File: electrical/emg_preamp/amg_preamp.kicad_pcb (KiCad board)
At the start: 2 copper layers, 29 x 13.5 mm, 26 parts, among them J1 in, J2 T1, J3 T2, J4 Conn_01x05, U1 TSZ124IPT

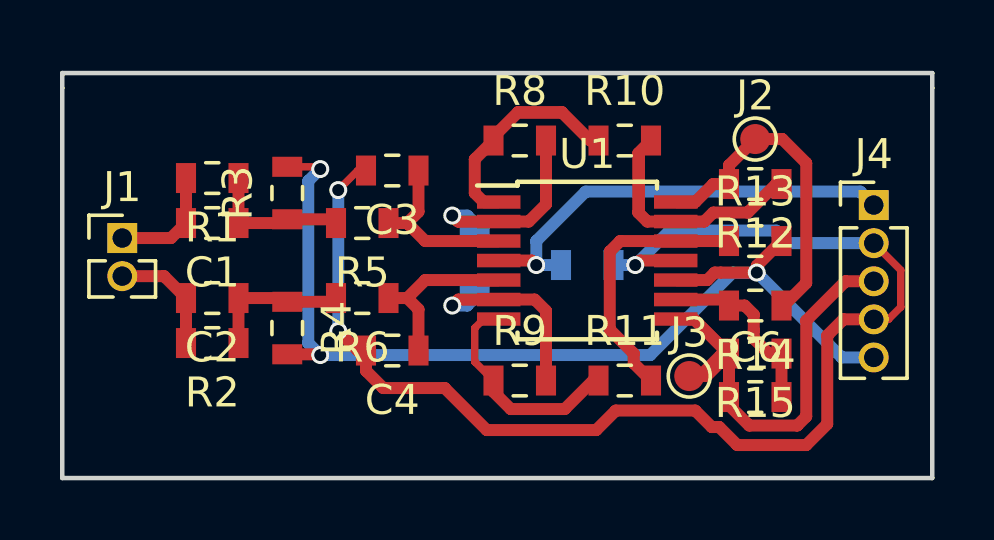
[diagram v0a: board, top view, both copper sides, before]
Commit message: Added output resistance to preamp board.
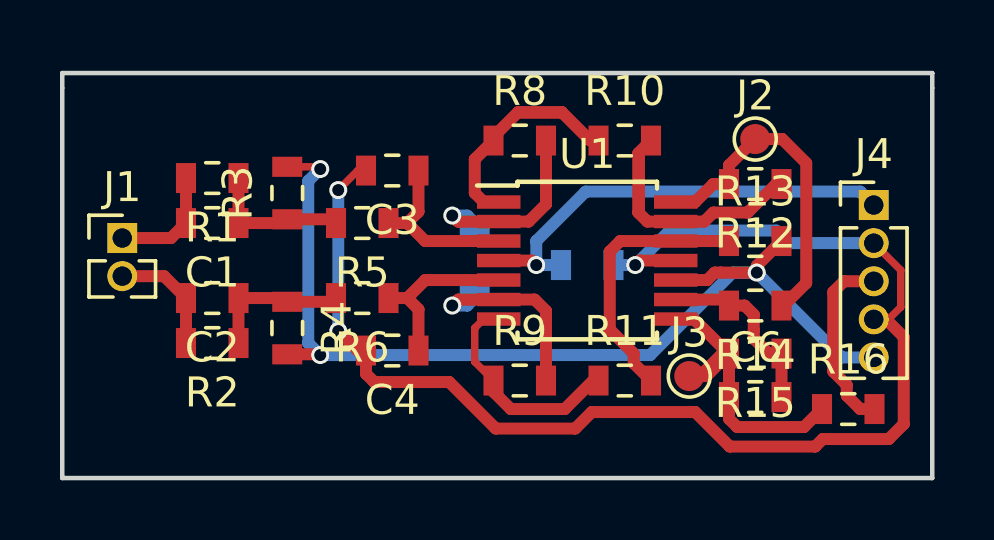
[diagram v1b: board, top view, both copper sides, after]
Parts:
- added R16: 1k 1%, Resistor_SMD:R_0603_1608Metric, F.Cu at (150.2, 105.7)
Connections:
- C6 pad 1: /out -> Net-(C6-Pad1)
- J3 pad 1: /out -> Net-(C6-Pad1)
- R15 pad 2: /out -> Net-(C6-Pad1)
- U1 pad 8: /out -> Net-(C6-Pad1)
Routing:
- net Net-(C6-Pad1): track 0.00 -> 13.7 mm
- net /out: track 18.5 -> 6.25 mm
- net GNDA: track 44.9 -> 46.9 mm

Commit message: Added filtering bypass caps.
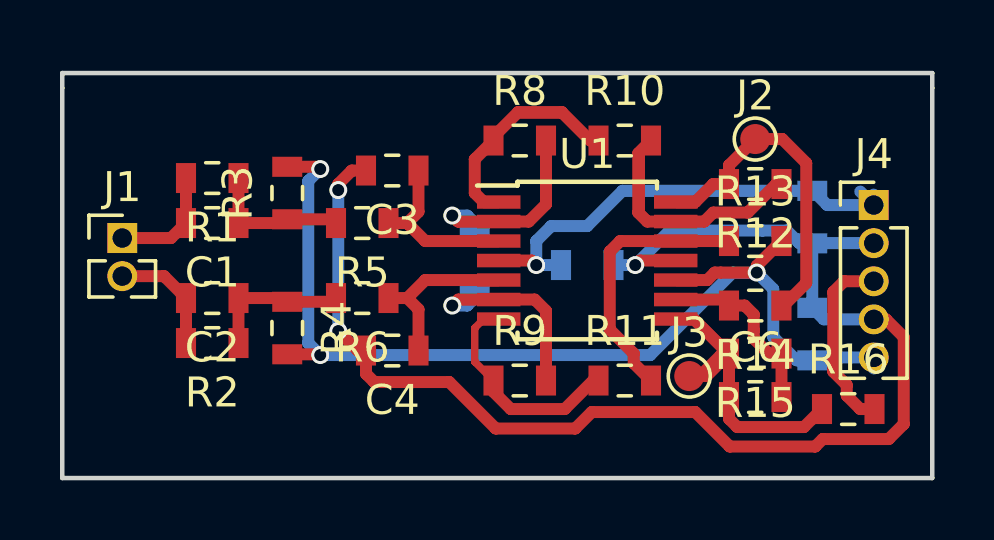
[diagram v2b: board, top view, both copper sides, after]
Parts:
- added C7: 100n, Capacitor_SMD:C_0603_1608Metric, B.Cu at (149.0, 99.3)
- added C8: 100n, Capacitor_SMD:C_0603_1608Metric, B.Cu at (149.0, 103.2)
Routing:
- net GNDA: track 46.9 -> 49.0 mm
- net /v_ref: track 35.7 -> 37.1 mm
- net VDDA: track 15.1 -> 16.1 mm
